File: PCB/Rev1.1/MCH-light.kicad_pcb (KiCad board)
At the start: 2 copper layers, 31 x 181.9 mm, 56 parts, among them J1 FTDI, J2 Barrel_Jack_Switch, J5 USB_B_Mini, J7 RJ45_Amphenol_RJMG1BD3B8K1ANR, J8 Screw_Terminal_01x03, J9 Screw_Terminal_01x03, SW1 Reset, SW2 Button, U1 AMS1117-3.3, U2 ESP32-WROOM-32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

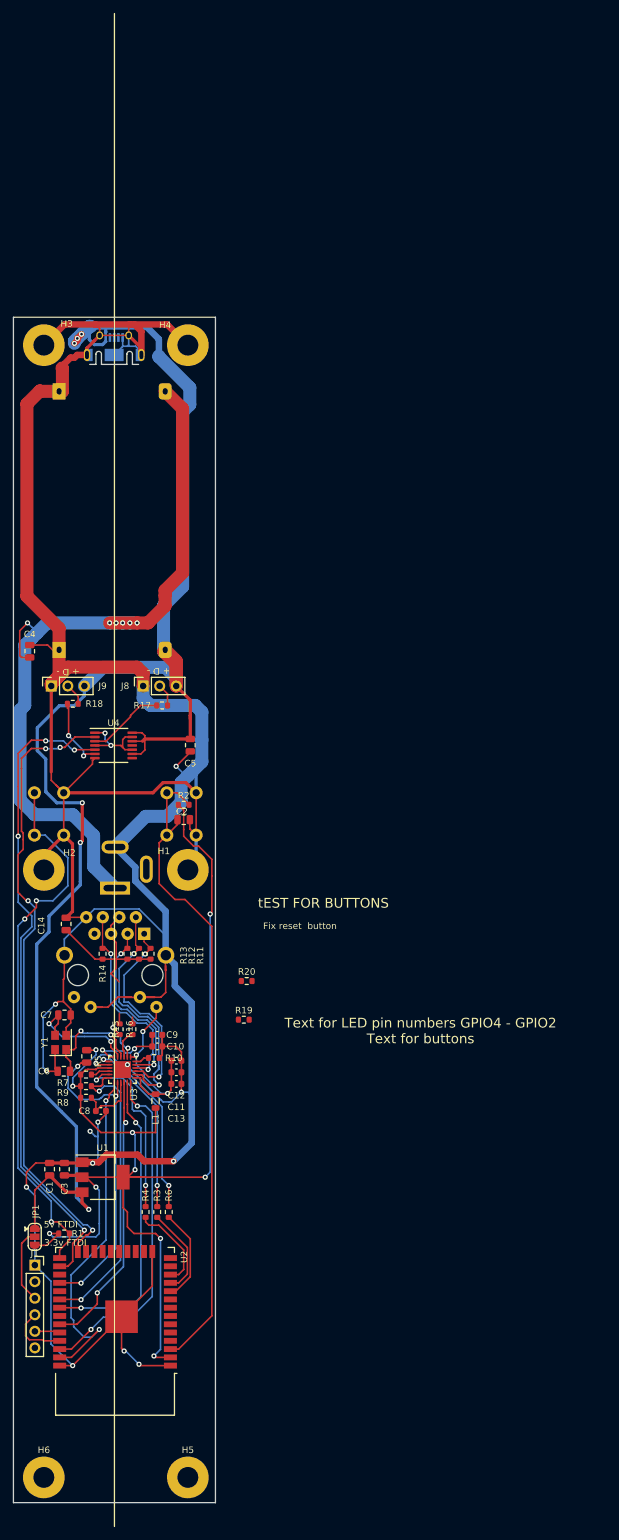
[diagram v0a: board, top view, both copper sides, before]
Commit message: routed updated pcb, added some more silk screen labling, :3
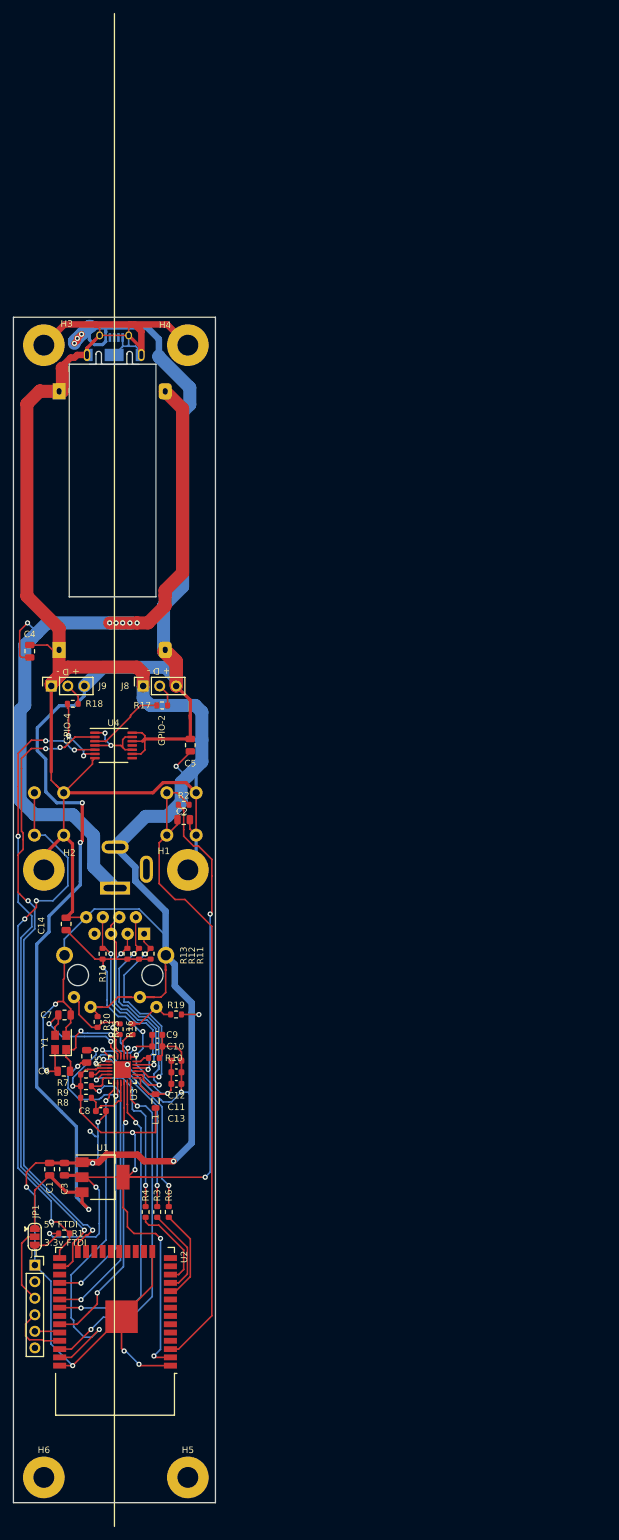
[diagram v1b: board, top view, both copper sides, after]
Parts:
- added REF**: OSHW-Logo2_24.3x20mm_SilkScreen, Symbol:OSHW-Logo2_24.3x20mm_SilkScreen, B.Cu at (130.1, 178.1)
- SW2: value Button -> Button - 0
- moved R20 23.7 mm to (127.2, 125.5), turned to -90 degrees
- moved R19 10.4 mm to (139.3, 124.4)
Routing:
- net Net-(J7-PadL1): track 1.64 -> 10.5 mm
- net Net-(J7-PadL4): track 1.02 -> 7.40 mm
- net GND: track 551.8 -> 557.7 mm, vias 13 -> 14
- net VDDA: track 56.8 -> 62.4 mm, vias 3 -> 4
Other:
- outline, holes or cut-outs redrawn
- board text added: "GPIO-2"
- board text added: "GPIO-4"
- board text removed: "Fix reset button"
- board text removed: "Text for LED pin numbers GPIO4 - GPIO2 Text for buttons"
- board text removed: "tEST FOR BUTTONS"
